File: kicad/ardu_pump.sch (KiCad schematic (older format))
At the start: 10 parts, among them J1 Conn_01x03_Male, J2 Conn_01x02_Female, J3 Conn_01x06_Male, Q1 Q_NPN_CBE, U1 ATtiny45-20PU, U2 HC-SR04

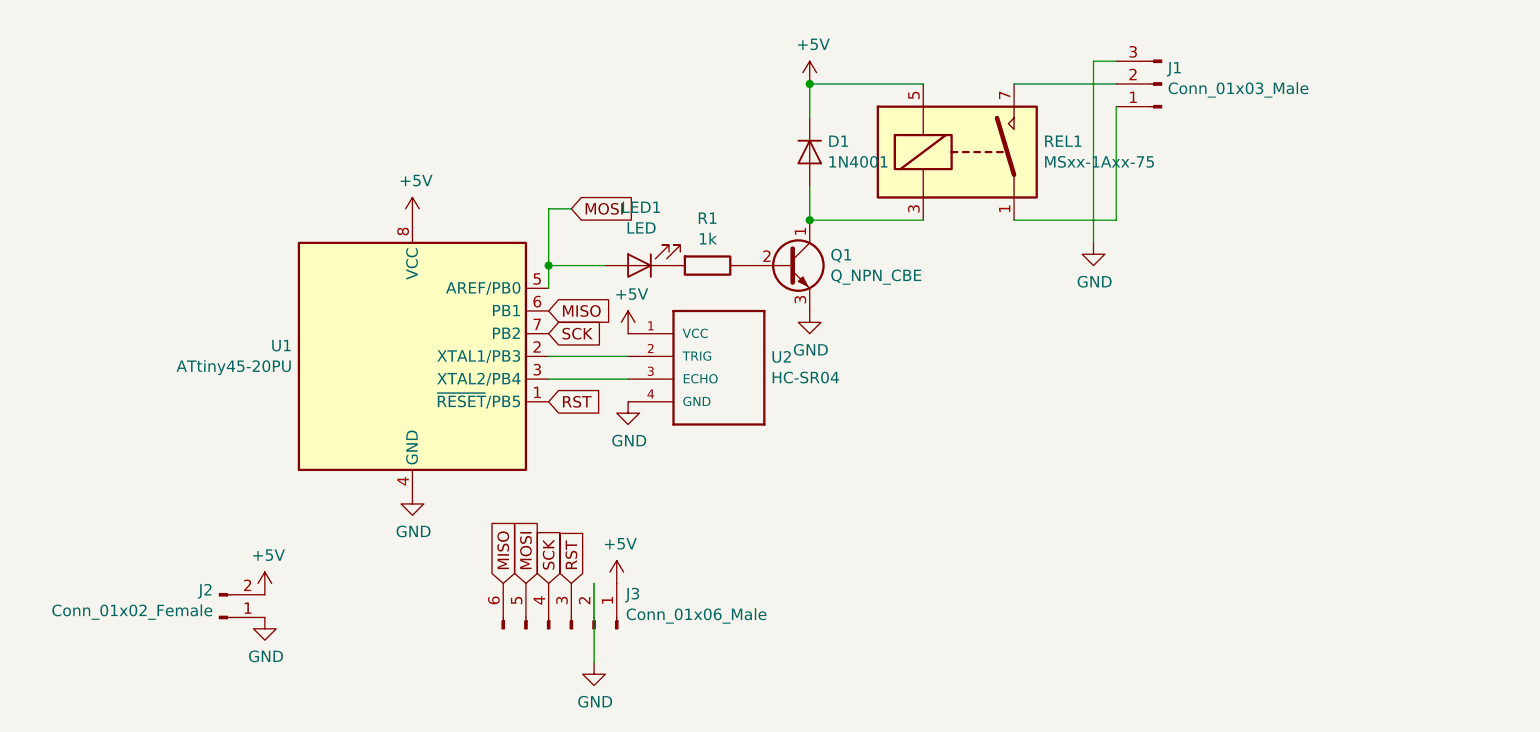
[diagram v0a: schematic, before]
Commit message: Improving schematic.
Adding buttons and more powerful relay.
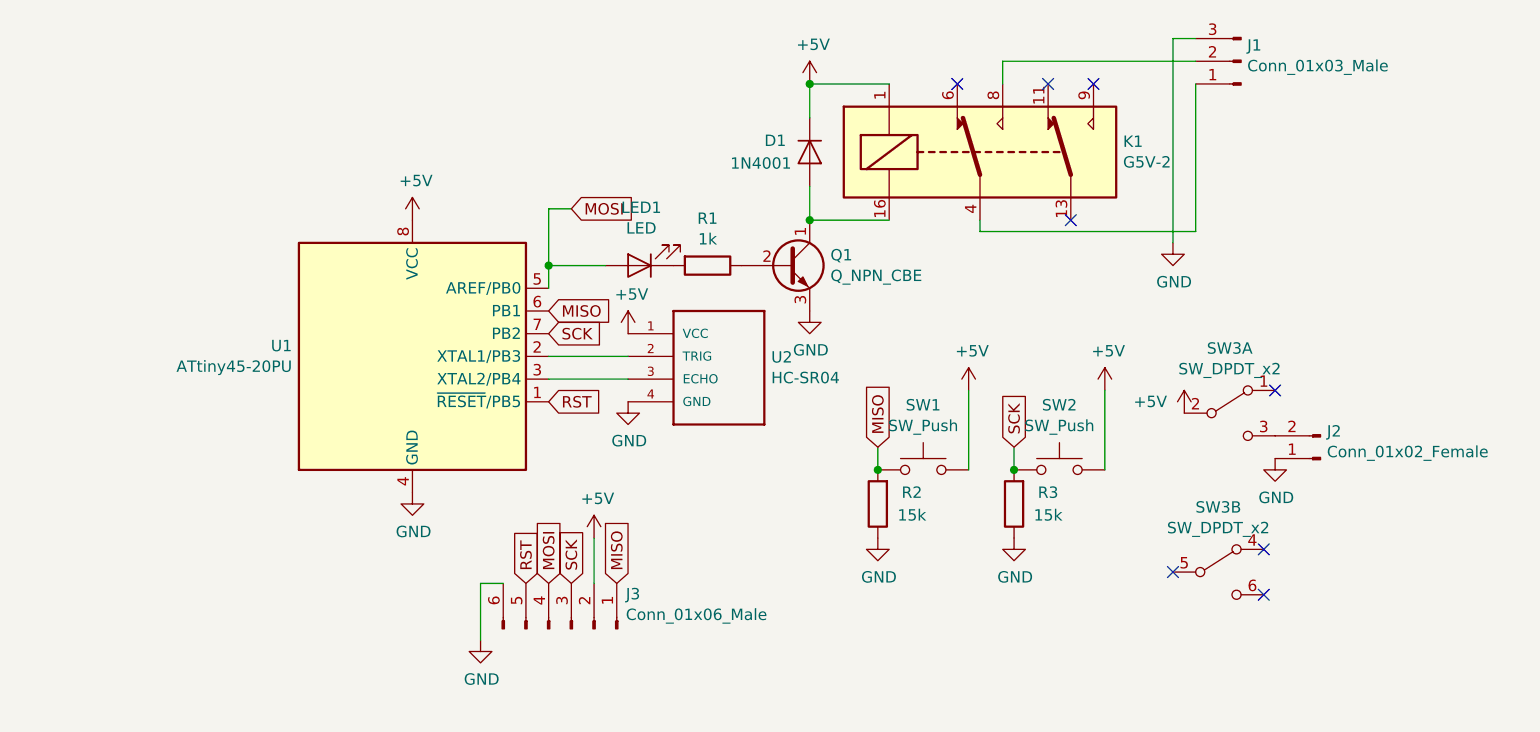
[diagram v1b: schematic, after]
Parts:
- removed REL1: MSxx-1Axx-75, Relay_THT:Relay_SPST_StandexMeder_MS_Form1AB, symbol Relay:MSxx-1Axx-75
- added K1: G5V-2, Relay_THT:Relay_DPDT_Omron_G5V-2, symbol Relay:G5V-2
- added R2, R3: 15k, Resistor_THT:R_Axial_DIN0207_L6.3mm_D2.5mm_P7.62mm_Horizontal, symbol Device:R
- added SW1, SW2: SW_Push, Button_Switch_THT:SW_Tactile_SPST_Angled_PTS645Vx58-2LFS, symbol Switch:SW_Push
- added SW3: SW_DPDT_x2, switch-dpdt:SW_PUSH_8x8mm_DPDT, symbol Switch:SW_DPDT_x2
- J1: footprint Connector_JST:JST_XH_B03B-XH-A_1x03_P2.50mm_Vertical -> Connector_JST:JST_XH_S03B-XH-A_1x03_P2.50mm_Horizontal
- J3: footprint Connector_PinHeader_2.54mm:PinHeader_1x06_P2.54mm_Horizontal -> Connector_IDC:IDC-Header_2x03_P2.54mm_Vertical
- R1: footprint Resistor_THT:R_Axial_DIN0207_L6.3mm_D2.5mm_P7.62mm_Horizontal -> Resistor_THT:R_Axial_DIN0207_L6.3mm_D2.5mm_P15.24mm_Horizontal
- U2: footprint Connector_PinSocket_2.54mm:PinSocket_1x04_P2.54mm_Vertical -> Connector_PinSocket_2.54mm:PinSocket_1x04_P2.54mm_Horizontal
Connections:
- net +5V: now also J3.2 (Pin_2), K1.1, SW1.2, SW2.2, SW3.2 (B); no longer J2.2 (Pin_2), J3.1 (Pin_1)
- net GND: now also J3.6 (Pin_6), R2.1, R3.1; no longer J3.2 (Pin_2)
- net MISO: now also J3.1 (Pin_1), R2.2, SW1.1; no longer J3.6 (Pin_6)
- net MOSI: now also J3.4 (Pin_4); no longer J3.5 (Pin_5)
- net RST: now also J3.5 (Pin_5); no longer J3.3 (Pin_3)
- net SCK: now also J3.3 (Pin_3), R3.2, SW2.1; no longer J3.4 (Pin_4)
- net at D1.2 (A), Q1.1 (C): now also K1.16
- net at J1.1 (Pin_1): now also K1.4
- net at J1.2 (Pin_2): now also K1.8
- new net: J2.2 (Pin_2), SW3.3 (C)
- no-connect marks 0 -> 8
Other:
- moved on the sheet: J1, J2
